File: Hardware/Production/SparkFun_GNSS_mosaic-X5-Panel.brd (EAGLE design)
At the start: 155.2 x 115.8 mm, 754 parts, among them J10 USB Female Type C Connector, J13 MICROSD, J21 USB Female Type C Connector, J23 MICROSD, J3 MICROSD, J31 USB Female Type C Connector, J33 MICROSD, J5 USB Female Type C Connector, Q1 20V/0.2A/8MHz/1.2Ω/1Vth, Q2 20V/0.2A/8MHz/1.2Ω/1Vth, Q3 20V/0.2A/8MHz/1.2Ω/1Vth, Q9 20V/0.2A/8MHz/1.2Ω/1Vth, T1 RFCMF1220100M4T, T2 RFCMF1220100M4T, T3 RFCMF1220100M4T, T4 RFCMF1220100M4T, U1 MOSAIC-X5X5, U10 3.3V, U11 MOSAIC-X5X5, U12 SN74AHC1G125DBVR, U2 SN74AHC1G125DBVR, U3 3.3V, U4 MOSAIC-X5X5, U5 3.3V, U6 SN74AHC1G125DBVR, U7 3.3V, U8 MOSAIC-X5X5, U9 SN74AHC1G125DBVR

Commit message: Add v11 panel.
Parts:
- added D45: RED, SparkFun-LED:LED-0603
- added D46: GREEN, SparkFun-LED:LED-0603
- added D47: ESD Diode, SparkFun-DiscreteSemi:SOT-23-6
- added D48, D49: 3A/10V/280mV, SparkFun-DiscreteSemi:SOD-323
- added D50: BLUE, SparkFun-LED:LED-0603
- added D51: WHITE, SparkFun-LED:LED-0603
- added D52, D53, D54, D55, D56: PESDXL4UGUG, SparkFun-DiscreteSemi:SOT353
- added R69, R70: 2.2k, SparkFun-Resistors:0603
- added R71: 0, SparkFun-Resistors:0603
- added R72: 10k, SparkFun-Resistors:0603
- D12: value PESD0402 -> PESDXL4UGUG; device SparkFun-DiscreteSemi:0402-TIGHT -> SparkFun-DiscreteSemi:SOT353
- D13, D24: value Yellow -> PESDXL4UGUG; device SparkFun-LED:LED-0603 -> SparkFun-DiscreteSemi:SOT353
- D14, D25: value RED -> PESDXL4UGUG; device SparkFun-LED:LED-0603 -> SparkFun-DiscreteSemi:SOT353
- D15: value GREEN -> PESD0402; device SparkFun-LED:LED-0603 -> SparkFun-DiscreteSemi:0402-TIGHT
- D16: value ESD Diode -> Yellow; device SparkFun-DiscreteSemi:SOT-23-6 -> SparkFun-LED:LED-0603
- D17: value 3A/10V/280mV -> RED; device SparkFun-DiscreteSemi:SOD-323 -> SparkFun-LED:LED-0603
- D18: value 3A/10V/280mV -> GREEN; device SparkFun-DiscreteSemi:SOD-323 -> SparkFun-LED:LED-0603
- D19: value BLUE -> ESD Diode; device SparkFun-LED:LED-0603 -> SparkFun-DiscreteSemi:SOT-23-6
- D20: value WHITE -> 3A/10V/280mV; device SparkFun-LED:LED-0603 -> SparkFun-DiscreteSemi:SOD-323
- D21: value PESDXL4UGUG -> 3A/10V/280mV; device SparkFun-DiscreteSemi:SOT353 -> SparkFun-DiscreteSemi:SOD-323
- D22: value PESDXL4UGUG -> BLUE; device SparkFun-DiscreteSemi:SOT353 -> SparkFun-LED:LED-0603
- D23: value PESD0402 -> WHITE; device SparkFun-DiscreteSemi:0402-TIGHT -> SparkFun-LED:LED-0603
- D26: value GREEN -> PESDXL4UGUG; device SparkFun-LED:LED-0603 -> SparkFun-DiscreteSemi:SOT353
- D27, D38: value ESD Diode -> PESDXL4UGUG; device SparkFun-DiscreteSemi:SOT-23-6 -> SparkFun-DiscreteSemi:SOT353
- D28, D39, D40: value 3A/10V/280mV -> PESDXL4UGUG; device SparkFun-DiscreteSemi:SOD-323 -> SparkFun-DiscreteSemi:SOT353
- D29: value 3A/10V/280mV -> PESD0402; device SparkFun-DiscreteSemi:SOD-323 -> SparkFun-DiscreteSemi:0402-TIGHT
- D30: value BLUE -> Yellow
- D31: value WHITE -> RED
- D32: value PESDXL4UGUG -> GREEN; device SparkFun-DiscreteSemi:SOT353 -> SparkFun-LED:LED-0603
- D33: value PESDXL4UGUG -> ESD Diode; device SparkFun-DiscreteSemi:SOT353 -> SparkFun-DiscreteSemi:SOT-23-6
- D34: value PESD0402 -> 3A/10V/280mV; device SparkFun-DiscreteSemi:0402-TIGHT -> SparkFun-DiscreteSemi:SOD-323
- D35: value Yellow -> 3A/10V/280mV; device SparkFun-LED:LED-0603 -> SparkFun-DiscreteSemi:SOD-323
- D36: value RED -> BLUE
- D37: value GREEN -> WHITE
- D41: value BLUE -> PESDXL4UGUG; device SparkFun-LED:LED-0603 -> SparkFun-DiscreteSemi:SOT353
- D42: value WHITE -> PESDXL4UGUG; device SparkFun-LED:LED-0603 -> SparkFun-DiscreteSemi:SOT353
- D43: value PESDXL4UGUG -> PESD0402; device SparkFun-DiscreteSemi:SOT353 -> SparkFun-DiscreteSemi:0402-TIGHT
- D44: value PESDXL4UGUG -> Yellow; device SparkFun-DiscreteSemi:SOT353 -> SparkFun-LED:LED-0603
- R14, R34: value 5.1k -> 10k
- R18, R35: value 2.2k -> 5.1k
- R19: value 1k -> 2.2k
- R20: value 330 -> 1k
- R21, R39, R59: value 10k -> 330
- R24, R41, R60, R65: value 1k -> 10k
- R25, R30, R50: value 2.2k -> 1k
- R26, R57: value 10k -> 2.2k
- R27, R45: value 169K -> 10k
- R29, R48: value 1k -> 169K
- R32, R51: value 0 -> 2.2k
- R33, R53: value 5.1k -> 0
- R36, R55: value 1k -> 5.1k
- R37: value 330 -> 2.2k
- R38, R43, R58: value 10k -> 1k
- R42, R54, R61: value 2.2k -> 10k
- R44, R64: value 169K -> 2.2k
- R49, R66, R67: value 2.2k -> 169K
- R52: value 5.1k -> 2.2k
- R56: value 330 -> 5.1k
- R63: value 169K -> 1k
- R68: value 0 -> 1k
- U$105: device output:#RTS_#5 -> output:COM40
- U$120: device output:#LOG#5 -> output:COM10
- U$126: device output:#LOG_LED_#5 -> output:#3#3V#1
- U$127: device output:#PMIC_#6 -> output:#GND#0
- U$128: device output:#GP_LED_#4 -> output:#3#3V#1
- U$129: device output:#RDY_#3 -> output:#GND#0
- U$139: device output:#RDY#3 -> output:##RST##2
- U$148: device output:#EVENTA_#9 -> output:#GP_LED#4
- U$149: device output:#EVENTB#11 -> output:#PMIC#6
- U$151: device output:#GP1_#2 -> output:#RDY#3
- U$153: device output:#GP2_#3 -> output:#VIN#1
- U$155: device output:#LOG_BTN_#5 -> output:#VUSB#0
- U$157: device output:#PPS_#7 -> output:#V_BAT#7
- U$161, U$269, U$377: device output:#RDY_#3 -> output:#_#RST##2
- U$162, U$270, U$378: device output:#VIN#1 -> output:L1#2#50
- U$163, U$271, U$379: device output:#VUSB#0 -> output:_ACTIVE_ANT1
- U$164, U$272, U$380: device output:#V_BAT#7 -> output:TIME0
- U$165, U$273, U$381: device output:#_#RST##2 -> output:PULSE1
- U$166, U$274, U$382: device output:#LOG_LED_#5 -> output:GNSS1
- U$167, U$275, U$383: device output:#PMIC_#6 -> output:TRIBAND2
- U$168, U$276, U$384: device output:#GP_LED_#4 -> output:#GP_LED#3
- U$169, U$277, U$385: device output:L1#2#50 -> output:#LOG_LED#2
- U$17: device output:#_RTK#0 -> output:#EVENTA#0
- U$170, U$278, U$386: device output:_ACTIVE_ANT1 -> output:#PPS_LED#1
- U$171, U$279, U$387: device output:TIME0 -> output:#PWR_LED#0
- U$172, U$280, U$388: device output:PULSE1 -> output:#V_BAT#4
- U$173, U$281, U$389: device output:GNSS1 -> output:#A#8
- U$174, U$282, U$390: device output:TRIBAND2 -> output:#B#10
- U$175, U$283, U$391: device output:#GP_LED#3 -> output:#GP1#0
- U$176, U$284, U$392: device output:#LOG_LED#2 -> output:#GP2#1
- U$177, U$285, U$393: device output:#PPS_LED#1 -> output:#LOG#4
- U$178, U$286, U$394: device output:#PWR_LED#0 -> output:#PPS#6
- U$179, U$287, U$395: device output:#V_BAT#4 -> output:GNSS_1
- U$180, U$288, U$396: device output:#A#8 -> output:TRIBAND_2
- U$181, U$289, U$397: device output:#B#10 -> output:MEAS0
- U$182, U$290, U$398: device output:#EVENTA_#9 -> output:C4
- U$183, U$291, U$399: device output:#EVENTB#11 -> output:D#2
- U$184, U$292, U$400: device output:#GP1#0 -> output:D#3
- U$185, U$293, U$401: device output:#GP1_#2 -> output:G0
- U$186, U$294, U$402: device output:#GP2#1 -> output:R5
- U$187, U$295, U$403: device output:#GP2_#3 -> output:RX7
- U$188, U$296, U$404: device output:#LOG#4 -> output:TX6
- U$189, U$297, U$405: device output:#LOG_BTN_#5 -> output:V8
- U$190, U$298, U$406: device output:#PPS#6 -> output:COM30
- U$191, U$299, U$407: device output:#PPS_#7 -> output:MOSAIC#X50
- U$192, U$300, U$408: device output:GNSS_1 -> output:MOSAIC#X5_0
- U$193, U$301, U$409: device output:TRIBAND_2 -> output:V0
- U$194, U$302, U$410: device output:MEAS0 -> output:G1
- U$195, U$303, U$411: device output:C4 -> output:#RTK#0
- U$196, U$304, U$412: device output:D#2 -> output:3V30
- U$197, U$305, U$413: device output:D#3 -> output:5V0
- U$198, U$306, U$414: device output:G0 -> output:#ANT_V#0
- U$199, U$307, U$415: device output:R5 -> output:#RTK_LED#0
- U$200, U$308, U$416: device output:RX7 -> output:RTK0
- U$201, U$309, U$417: device output:TX6 -> output:PVT0
- U$202, U$310, U$418: device output:V8 -> output:#GP1_#0
- U$203, U$311, U$419: device output:COM30 -> output:#GP2_#0
- U$204, U$312, U$420: device output:MOSAIC#X50 -> output:#PPS_#0
- U$205, U$313, U$421: device output:MOSAIC#X5_0 -> output:#LOG_BTN#0
- U$206, U$314, U$422: device output:V0 -> output:#LOG_L#0
- U$207, U$315, U$423: device output:G1 -> output:#RDY#0
- U$208, U$316, U$424: device output:#RTK#0 -> output:#GP_LED#0
- U$209, U$317, U$425: device output:#_RTK#0 -> output:#LOG_LED#0
- U$210, U$318, U$426: device output:3V30 -> output:#PMIC#0
- U$211, U$319, U$427: device output:5V0 -> output:#RTS#0
- U$212, U$320, U$428: device output:#ANT_V#0 -> output:#RTS#0
- U$213, U$321, U$429: device output:#RTK_LED#0 -> output:#RTK_#0
- U$214, U$322, U$430: device output:RTK0 -> output:#EVENTA#0
- U$215, U$323, U$431: device output:PVT0 -> output:#EVENTB#0
- U$216, U$324, U$432: device output:MADE_IN_AMERICA0 -> output:MADE_IN_THE_USA0
- U$239, U$347: device output:#RTS_#5 -> output:#RX_#2
- U$240, U$348: device output:#RX_#2 -> output:#TX_#3
- U$241, U$349: device output:#TX_#3 -> output:#CTS#4
- U$242, U$350: device output:#CTS#4 -> output:#RTS#5
- U$243, U$351: device output:#RTS#5 -> output:#RX#2
- U$244, U$352: device output:#RX#2 -> output:#TX#3
- U$245, U$353: device output:#TX#3 -> output:#CTS_#4
- U$246, U$354: device output:#CTS_#4 -> output:#RX_#2
- U$247, U$355: device output:#RTS_#5 -> output:#TX_#3
- U$248, U$356: device output:#RX_#2 -> output:#RX#2
- U$249, U$357: device output:#TX_#3 -> output:#TX#3
- U$250, U$358: device output:#RX#2 -> output:#RX_#2
- U$251, U$359: device output:#TX#3 -> output:#TX_#3
- U$252, U$360, U$54: device output:#RX_#2 -> output:COM20
- U$253, U$361: device output:#TX_#3 -> output:COM40
- U$254, U$362: device output:COM20 -> output:COM10
- U$255, U$363: device output:COM40 -> output:#3#3V#1
- U$256, U$364: device output:COM10 -> output:#GND#0
- U$259, U$367: device output:#3#3V#1 -> output:##RST##2
- U$260, U$368: device output:#GND#0 -> output:#GP_LED#4
- U$261, U$369: device output:##RST##2 -> output:#PMIC#6
- U$262, U$370: device output:#GP_LED#4 -> output:#RDY#3
- U$263, U$371: device output:#LOG#5 -> output:#VIN#1
- U$264, U$372: device output:#PMIC#6 -> output:#VUSB#0
- U$265, U$373: device output:#RDY#3 -> output:#V_BAT#7
- U$30: device output:MADE_IN_AMERICA0 -> output:#GP1_#0
- U$33: device output:L1#2#50 -> output:#GP2_#0
- U$34: device output:_ACTIVE_ANT1 -> output:#PPS_#0
- U$35: device output:RST0 -> output:#LOG_BTN#0
- U$36: device output:LOG0 -> output:#LOG_L#0
- U$37: device output:LOG2 -> output:#RDY#0
- U$38: device output:PPS0 -> output:#GP_LED#0
- U$39: device output:PWR3 -> output:#LOG_LED#0
- U$40: device output:COM30 -> output:#PMIC#0
- U$41: device output:COM20 -> output:#RTS#0
- U$42: device output:COM10 -> output:#RTS#0
- U$43: device output:COM40 -> output:#RTK_#0
- U$44: device output:#3#3V#1 -> output:#EVENTB#0
- U$45: device output:#CTS#4 -> output:MADE_IN_THE_USA0
- U$46: device output:#GND#0 -> output:L1#2#50
- U$47: device output:#RTS#5 -> output:_ACTIVE_ANT1
- U$48: device output:#RX#2 -> output:RST0
- U$49: device output:#TX#3 -> output:LOG0
- U$50: device output:#3#3V#1 -> output:LOG2
- U$51: device output:#CTS_#4 -> output:PPS0
- U$52: device output:#GND#0 -> output:PWR3
- U$53: device output:#RTS_#5 -> output:COM30
- U$55: device output:#TX_#3 -> output:COM10
- U$56: device output:#CTS#4 -> output:COM40
- U$57: device output:#RTS#5 -> output:#3#3V#1
- U$58: device output:#RX#2 -> output:#CTS#4
- U$59, U$65: device output:#TX#3 -> output:#GND#0
- U$60: device output:#CTS_#4 -> output:#RTS#5
- U$61: device output:#RTS_#5 -> output:#RX#2
- U$62: device output:#RX_#2 -> output:#TX#3
- U$63: device output:#TX_#3 -> output:#3#3V#1
- U$64: device output:#RX#2 -> output:#CTS_#4
- U$68: device output:COM20 -> output:#CTS#4
- U$70: device output:COM40 -> output:#RTS#5
- U$71: device output:COM10 -> output:#RX#2
- U$72: device output:#3#3V#1 -> output:#TX#3
- U$73: device output:#GND#0 -> output:#CTS_#4
- U$74: device output:#3#3V#1 -> output:#RX_#2
- U$75: device output:#GND#0 -> output:#TX_#3
- U$76: device output:##RST##2 -> output:#RX#2
- U$77: device output:#GP_LED#4 -> output:#TX#3
- U$78: device output:#LOG#5 -> output:#RX_#2
- U$86: device output:#PMIC#6 -> output:#TX_#3
- U$96: device output:#RTS_#5 -> output:COM20
- moved D28 121.9 mm to (108.5, 7.62), turned to 270 degrees
- moved R34 120.6 mm to (116.1, 7.62), turned to 0 degrees
- moved D35 112.9 mm to (8.89, 67.8), turned to 180 degrees
- moved D34 112.6 mm to (8.89, 78.0), turned to 180 degrees
- moved D13 103.8 mm to (21.6, 7.62), turned to 270 degrees
- moved D41 102.5 mm to (21.6, 58.9), turned to 270 degrees
- moved D26 101.5 mm to (98.3, 7.62), turned to 270 degrees
- moved R33 100.6 mm to (109.7, 43.2), turned to 270 degrees
- moved D27 94.8 mm to (88.1, 7.62), turned to 270 degrees
- moved D12 93.5 mm to (31.8, 7.62)
- moved U$33 90.7 mm to (43.2, 3.68), flipped to the bottom, turned to 270 degrees
- moved U$37 88.1 mm to (33.0, 46.7), flipped to the bottom, turned to 270 degrees
- moved D14 86.3 mm to (41.9, 7.62), turned to 270 degrees
- moved U$38 85.5 mm to (35.6, 45.2), flipped to the bottom, turned to 270 degrees
- moved U$39 83.3 mm to (38.1, 44.7), flipped to the bottom, turned to 270 degrees
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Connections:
- removed net ICM-20948-LV_#_1.8V: Q9.1, R46.2
- removed net ICM-20948-LV_#_1.8V1: Q1.1, R30.2
- removed net ICM-20948-LV_#_1.8V2: Q2.1, R49.2
- removed net ICM-20948-LV_#_1.8V3: Q3.1, R66.2
- net !RESET!: now also D9.3
- net !RESET!1: now also D24.3
- net !RESET!2: now also D38.3
- net !RESET!3: now also D52.3
- net 1.8V: now also Q9.1, R46.2
- net 1.8V1: now also Q1.1, R22.2, R31.2; no longer R21.2
- net 1.8V2: now also Q2.1, R40.2, R51.2; no longer R38.2
- net 1.8V3: now also Q3.1, R60.2, R69.2; no longer R57.2
- net 3.3V: now also R14.2
- net 3.3V1: now also R24.2, R27.2, R32.2, R34.2; no longer R22.2, R26.2, R31.2
- net 3.3V2: now also R41.2, R42.2, R45.2, R52.2, R54.2; no longer R39.2, R40.2, R43.2, R50.2
- net 3.3V3: now also R61.2, R65.2, R70.2, R72.2; no longer R58.2, R59.2, R67.2
- net ANT_V1: now also R33.1; no longer R32.1
- net ANT_V2: now also R53.1; no longer R51.1
- net ANT_V3: now also R71.1; no longer R68.1
- net CC3: now also R18.2; no longer R15.2
- net CC4: now also R15.2; no longer R14.2
- net CC5: now also R36.2; no longer R34.2
- net CC6: now also R35.2; no longer R33.2
- net CC7: now also R56.2; no longer R53.2
- net CC8: now also R55.2; no longer R52.2
- net COM1_CTS: now also D13.4
- net COM1_CTS1: now also D27.4
- net COM1_CTS2: now also D41.4
- net COM1_CTS3: now also D55.4
- net COM1_RTS: now also D13.3
- net COM1_RTS1: now also D27.3
- net COM1_RTS2: now also D41.3
- net COM1_RTS3: now also D55.3
- net COM1_RX: now also D13.1
- net COM1_RX1: now also D27.1
- net COM1_RX2: now also D41.1
- net COM1_RX3: now also D55.1
- net COM1_TX: now also D13.5
- net COM1_TX1: now also D27.5
- net COM1_TX2: now also D41.5
- net COM1_TX3: now also D55.5
- net COM2_CTS: now also D12.5
- net COM2_CTS1: now also D26.5
- net COM2_CTS2: now also D40.5
- net COM2_CTS3: now also D54.5
- net COM2_RTS: now also D12.1
- net COM2_RTS1: now also D26.1
- net COM2_RTS2: now also D40.1
- net COM2_RTS3: now also D54.1
- net COM2_RX: now also D12.3
- net COM2_RX1: now also D26.3
- net COM2_RX2: now also D40.3
- net COM2_RX3: now also D54.3
- net COM2_TX: now also D12.4
- net COM2_TX1: now also D26.4
- net COM2_TX2: now also D40.4
- net COM2_TX3: now also D54.4
- net COM3_CTS1: now also D25.5; no longer D22.5
- net COM3_CTS2: now also D39.5; no longer D33.5
- net COM3_CTS3: now also D53.5; no longer D44.5
- net COM3_RTS1: now also D25.4; no longer D22.4
- net COM3_RTS2: now also D39.4; no longer D33.4
- net COM3_RTS3: now also D53.4; no longer D44.4
- net COM3_RX1: now also D25.1; no longer D22.1
- net COM3_RX2: now also D39.1; no longer D33.1
- net COM3_RX3: now also D53.1; no longer D44.1
- net COM3_TX1: now also D25.3; no longer D22.3
- net COM3_TX2: now also D39.3; no longer D33.3
- net COM3_TX3: now also D53.3; no longer D44.3
- net COM4_RX: now also D14.1
- net COM4_RX1: now also D28.1
- net COM4_RX2: now also D42.1
- net COM4_RX3: now also D56.1
- net COM4_TX: now also D14.3
- net COM4_TX1: now also D28.3
- net COM4_TX2: now also D42.3
- net COM4_TX3: now also D56.3
- net EVENTA1: now also R28.2; no longer R27.2
- net EVENTA2: now also R48.2; no longer R44.2
- net EVENTA3: now also R66.2; no longer R63.2
- net EVENTB1: now also R29.2; no longer R28.2
- net EVENTB2: now also R49.2; no longer R45.2
- net EVENTB3: now also R67.2; no longer R64.2
- net GND: now also D12.2, D13.2, D14.2
- net GND1: now also D15.2, D16.C, D17.C, D18.C, D19.2, D22.C, D23.C, D24.2, D25.2, D26.2, D27.2, D28.2, R18.1; no longer D12.2, D13.C, D14.C, D15.C, D16.2, D19.C, D20.C, D21.2, D22.2, R14.1
- net GND2: now also D29.2, D32.C, D36.C, D37.C, D38.2, D39.2, D40.2, D41.2, D42.2, R35.1, R36.1; no longer D23.2, D24.C, D25.C, D26.C, D27.2, D32.2, R33.1, R34.1
- net GND3: now also D44.C, D45.C, D46.C, D47.2, D50.C, D51.C, D52.2, D53.2, D54.2, D55.2, D56.2, R55.1, R56.1; no longer D34.2, D35.C, D36.C, D37.C, D38.2, D41.C, D42.C, D44.2, R52.1, R53.1
- net GP1: now also D14.4
- net GP2: now also D14.5
- net GP3: now also D28.4
- net GP4: now also D28.5
- net GP5: now also D42.4
- net GP6: now also D42.5
- net GP7: now also D56.4
- net GP8: now also D56.5
- net GPS_ANT2: now also D15.1; no longer D12.1
- net GPS_ANT3: now also D29.1; no longer D23.1
- net GPS_ANT4: now also D43.1; no longer D34.1
- net LOG_BTN: now also R14.1
- net LOG_BTN1: now also R25.2, R34.1; no longer R24.2
- net LOG_BTN2: now also R43.2, R54.1; no longer R41.2
- net LOG_BTN3: now also R63.2, R72.1; no longer R60.2
- net MEAS1: now also D20.C, D21.C; no longer D17.C, D18.C
- net MEAS2: now also D34.C, D35.C; no longer D28.C, D29.C
- net MEAS3: now also D48.C, D49.C; no longer D39.C, D40.C
- net N$13: now also D16.A, R19.1; no longer D13.A, R18.1
- net N$18: now also R19.2; no longer R18.2
- net N$19: now also D17.A, R20.1; no longer D14.A, R19.1
- net N$21: now also D18.A, R21.1; no longer D15.A, R20.1
- net N$22: now also R21.2; no longer R20.2
- net N$23: now also R20.2; no longer R19.2
- net N$27: now also R22.1; no longer R21.1
- net N$28: now also R25.1; no longer R24.1
- net N$29: now also D22.A, R26.1; no longer D19.A, R25.1
- net N$30: now also R26.2; no longer R25.2
- net N$32: now also R27.1; no longer R26.1
- net N$33: now also R28.1; no longer R27.1
- net N$34: now also R29.1; no longer R28.1
- net N$35: now also D23.A, R30.1; no longer D20.A, R29.1
- net N$36: now also R30.2; no longer R29.2
- net N$37: now also D30.A, R37.1; no longer D24.A, R35.1
- net N$38: now also R37.2; no longer R35.2
- net N$39: now also D31.A, R38.1; no longer D25.A, R36.1
- net N$40: now also D32.A, R39.1; no longer D26.A, R37.1
- net N$41: now also R39.2; no longer R37.2
- net N$42: now also R38.2; no longer R36.2
- net N$45: now also R40.1; no longer R38.1
- net N$46: now also R43.1; no longer R41.1
- net N$47: now also D36.A, R44.1; no longer D30.A, R42.1
- net N$48: now also R44.2; no longer R42.2
- net N$50: now also R45.1; no longer R43.1
- net N$51: now also R48.1; no longer R44.1
- net N$52: now also R49.1; no longer R45.1
- net N$53: now also D37.A, R50.1; no longer D31.A, R48.1
- net N$54: now also R50.2; no longer R48.2
- net N$55: now also D44.A, R57.1; no longer D35.A, R54.1
- net N$56: now also R57.2; no longer R54.2
- net N$57: now also D45.A, R58.1; no longer D36.A, R55.1
- net N$58: now also D46.A, R59.1; no longer D37.A, R56.1
- net N$59: now also R59.2; no longer R56.2
- net N$60: now also R58.2; no longer R55.2
- net N$63: now also R60.1; no longer R57.1
- net N$64: now also R63.1; no longer R60.1
- net N$65: now also D50.A, R64.1; no longer D41.A, R61.1
- net N$66: now also R64.2; no longer R61.2
- net N$68: now also R65.1; no longer R62.1
- net N$69: now also R66.1; no longer R63.1
- net N$70: now also R67.1; no longer R64.1
- net N$71: now also D51.A, R68.1; no longer D42.A, R65.1
- net N$72: now also R68.2; no longer R65.2
- net PPS_1: now also R32.1; no longer R31.1
- net PPS_1V1: now also R31.1; no longer R30.1
- net PPS_1V2: now also R51.1; no longer R49.1
- net PPS_1V3: now also R69.1; no longer R66.1
- net PPS_2: now also R52.1; no longer R50.1
- net PPS_4: now also R70.1; no longer R67.1
- net SD_CLK1: now also D24.5; no longer D21.5
- net SD_CLK2: now also D38.5; no longer D32.5
- net SD_CLK3: now also D52.5; no longer D43.5
- net SD_CMD1: now also D24.4, R23.1; no longer D21.4, R22.1
- net SD_CMD2: now also D38.4, R41.1; no longer D32.4, R39.1
- net SD_CMD3: now also D52.4, R61.1; no longer D43.4, R58.1
- net SD_DATA1: now also D24.1, R24.1; no longer D21.1, R23.1
- net SD_DATA2: now also D38.1, R42.1; no longer D32.1, R40.1
- net SD_DATA3: now also D52.1, R62.1; no longer D43.1, R59.1
- net USB_D+1: now also D19.6; no longer D16.6
- net USB_D+2: now also D33.6; no longer D27.6
- net USB_D+3: now also D47.6; no longer D38.6
- net USB_D-1: now also D19.4; no longer D16.4
- net USB_D-2: now also D33.4; no longer D27.4
- net USB_D-3: now also D47.4; no longer D38.4
- net VANT1: now also R33.2; no longer R32.2
- net VANT2: now also R53.2; no longer R51.2
- net VANT3: now also R71.2; no longer R68.2
- net VIN1: now also D20.A; no longer D17.A
- net VIN2: now also D34.A; no longer D28.A
- net VIN3: now also D48.A; no longer D39.A
- net V_USB1: now also D19.5, D21.A; no longer D16.5, D18.A
- net V_USB2: now also D33.5, D35.A; no longer D27.5, D29.A
- net V_USB3: now also D47.5, D49.A; no longer D38.5, D40.A
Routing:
- net 1.8V1: track 6.61 -> 32.7 mm, vias 0 -> 2
- net 1.8V3: track 6.61 -> 32.7 mm, vias 0 -> 2
- net 1.8V: track 6.61 -> 32.7 mm, vias 0 -> 2
- net 1.8V2: track 6.61 -> 32.7 mm, vias 0 -> 2
- net 3.3V3: track 169.1 -> 188.7 mm, vias 6 -> 7
- net 3.3V2: track 169.1 -> 188.7 mm, vias 6 -> 7
- net 3.3V1: track 169.1 -> 188.7 mm, vias 6 -> 7
- net 3.3V: track 169.1 -> 188.7 mm, vias 6 -> 7
- net COM2_RX1: track 11.7 -> 23.9 mm, vias 0 -> 1
- net COM2_RX: track 11.7 -> 23.9 mm, vias 0 -> 1
- net COM2_RX3: track 11.7 -> 23.9 mm, vias 0 -> 1
- net COM2_RX2: track 11.7 -> 23.9 mm, vias 0 -> 1
- net COM4_RX1: track 35.4 -> 45.8 mm
- net COM4_RX: track 35.4 -> 45.8 mm
- net COM4_RX3: track 35.4 -> 45.8 mm
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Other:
- board text added: "v11"
- board text removed: "v10"

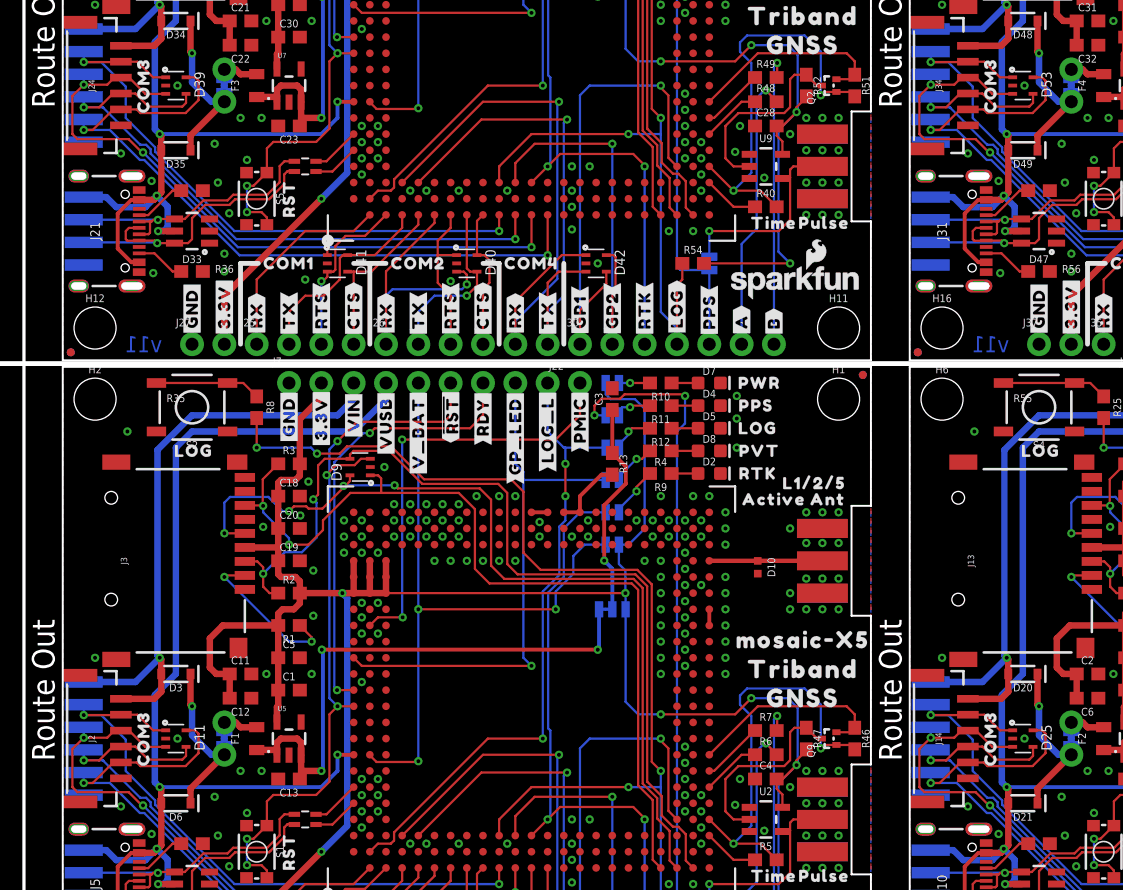
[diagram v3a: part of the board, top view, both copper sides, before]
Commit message: Swap CTS/RTS on COM3 JST connector.
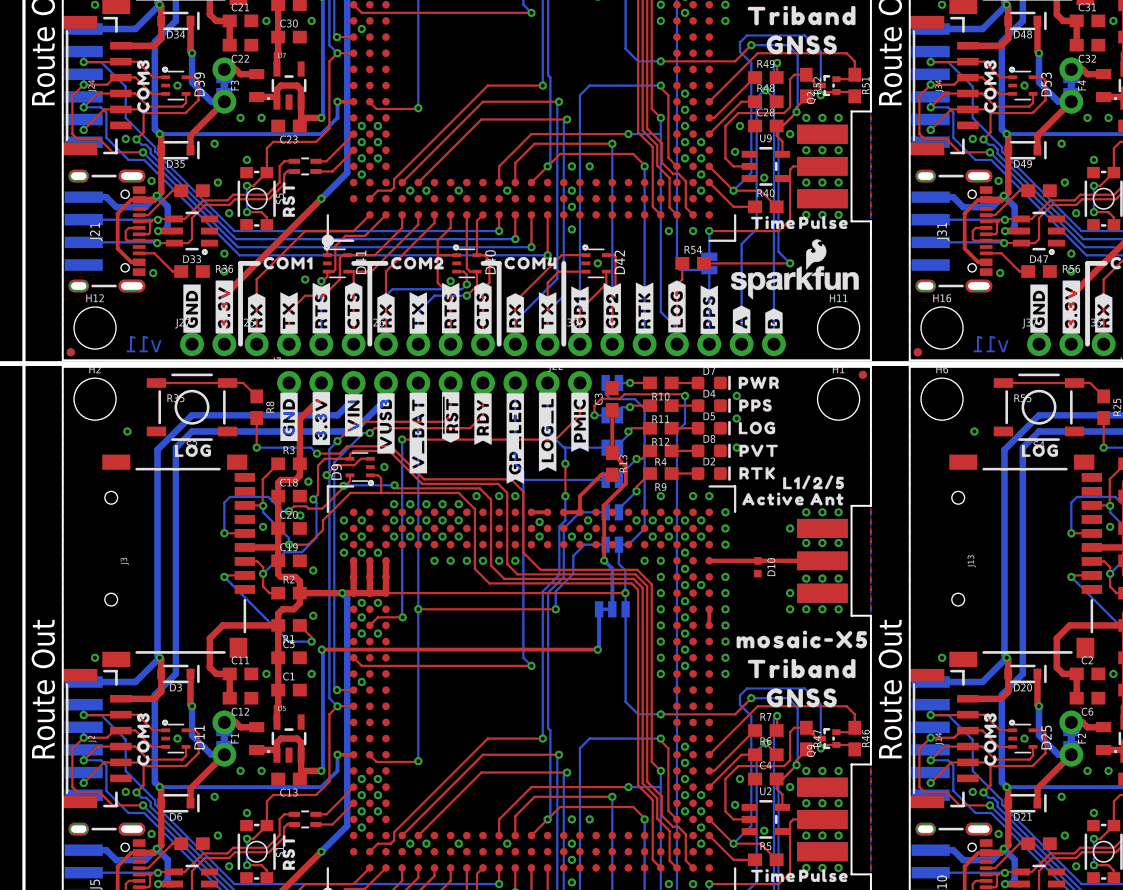
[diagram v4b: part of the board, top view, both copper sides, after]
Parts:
- moved U$402 1.78 mm to (70.7, 70.2)
- moved U$294 1.78 mm to (4.19, 70.2)
- moved U$186 1.78 mm to (70.7, 18.9)
- moved U$12 1.78 mm to (4.19, 18.9)
- moved U$290 1.78 mm to (4.19, 72.0)
- moved U$398 1.78 mm to (70.7, 72.0)
- moved U$182 1.78 mm to (70.7, 20.7)
- moved U$8 1.78 mm to (4.19, 20.7)
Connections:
- net COM3_CTS: now also D11.4, J12.4, J2.4; no longer D11.5, J12.5, J2.5
- net COM3_CTS1: now also D25.4, J14.4, J19.4; no longer D25.5, J14.5, J19.5
- net COM3_CTS2: now also D39.4, J24.4, J29.4; no longer D39.5, J24.5, J29.5
- net COM3_CTS3: now also D53.4, J34.4, J39.4; no longer D53.5, J34.5, J39.5
- net COM3_RTS: now also D11.5, J12.5, J2.5; no longer D11.4, J12.4, J2.4
- net COM3_RTS1: now also D25.5, J14.5, J19.5; no longer D25.4, J14.4, J19.4
- net COM3_RTS2: now also D39.5, J24.5, J29.5; no longer D39.4, J24.4, J29.4
- net COM3_RTS3: now also D53.5, J34.5, J39.5; no longer D53.4, J34.4, J39.4
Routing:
- net COM3_CTS: track 57.4 -> 56.2 mm
- net COM3_CTS1: track 57.4 -> 56.2 mm
- net COM3_CTS3: track 57.4 -> 56.2 mm
- net COM3_CTS2: track 57.4 -> 56.2 mm
- net COM3_RTS: track 50.9 -> 51.1 mm, vias 2 -> 3
- net COM3_RTS2: track 50.9 -> 51.1 mm, vias 2 -> 3
- net COM3_RTS3: track 50.9 -> 51.1 mm, vias 2 -> 3
- net COM3_RTS1: track 50.9 -> 51.1 mm, vias 2 -> 3

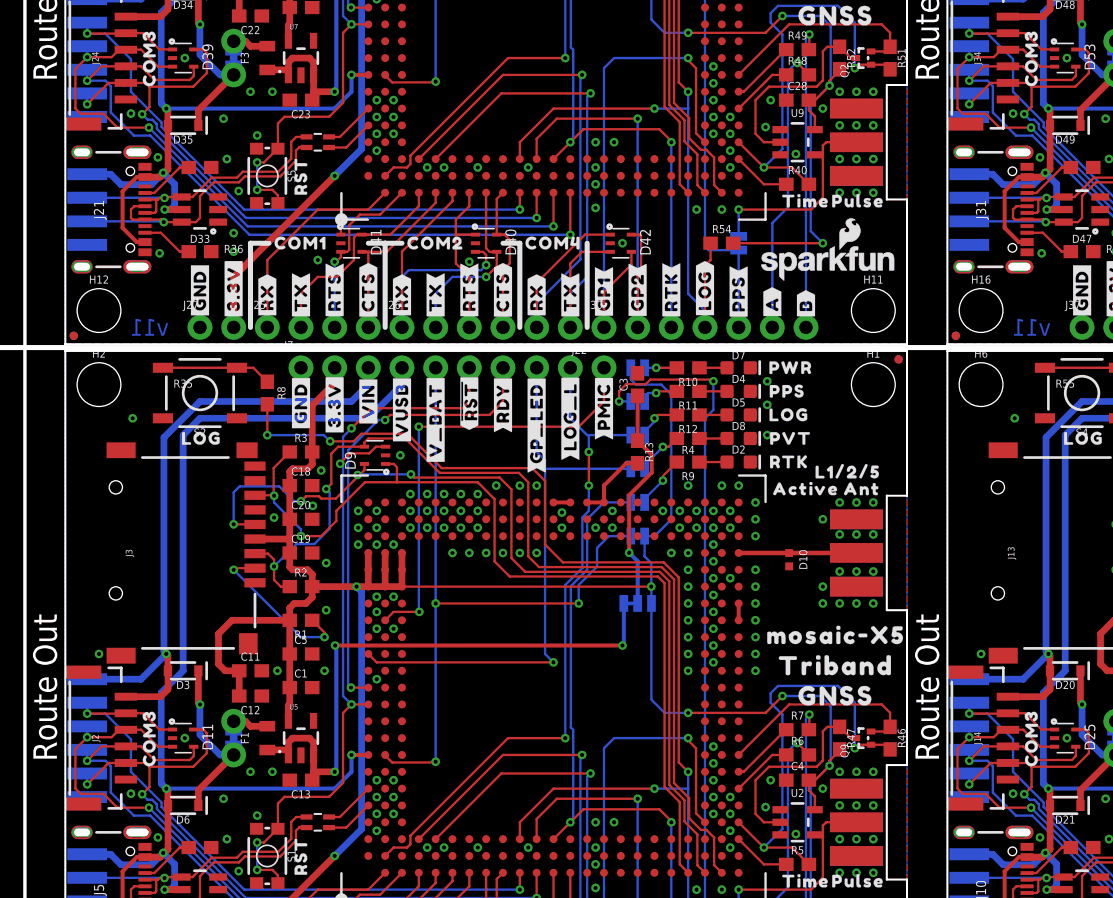
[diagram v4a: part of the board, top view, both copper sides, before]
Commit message: Update board measurements.
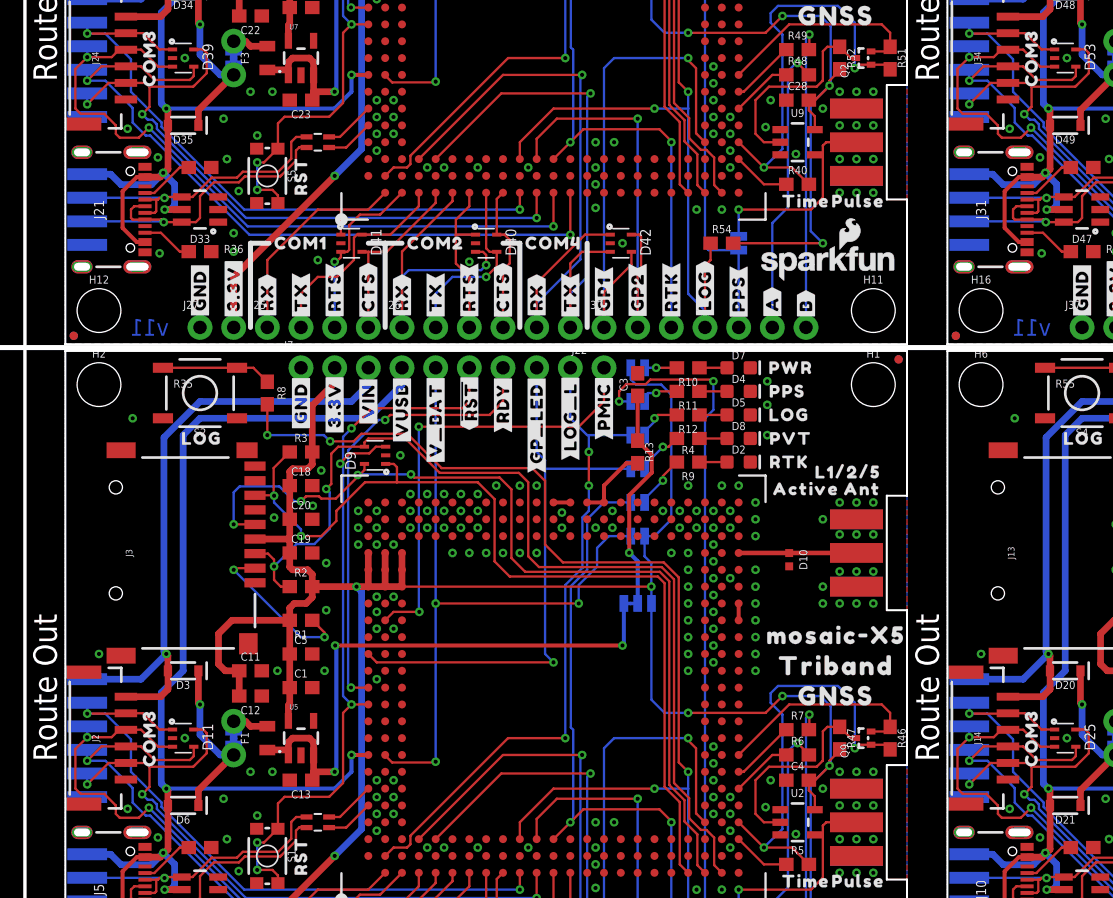
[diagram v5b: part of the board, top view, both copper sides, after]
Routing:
- net COM3_TX: track 54.6 -> 55.6 mm
- net COM3_TX1: track 54.6 -> 55.6 mm
- net COM3_TX2: track 54.6 -> 55.6 mm
- net COM3_TX3: track 54.6 -> 55.6 mm
- net COM3_CTS1: track 56.2 -> 55.6 mm
- net COM3_CTS3: track 56.2 -> 55.6 mm
- net COM3_CTS2: track 56.2 -> 55.6 mm
- net COM3_CTS: track 56.2 -> 55.6 mm

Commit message: Remove "Made in the USA" silk - for foreign PCB manufacture
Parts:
- removed U$216, U$324, U$432, U$45: (no value), output:MADE_IN_THE_USA0
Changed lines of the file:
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@@
 <attribute name="VALUE" x="39.37" y="8.89" size="0.8128" layer="27" rot="R270"/>
 </element>
-<element name="U$45" library="output" package="MADE_IN_THE_USA0" value="" x="19.05" y="11.43" smashed="yes" rot="MR0"/>
 <element name="JP2" library="SparkFun-Aesthetics" package="FIDUCIAL-MICRO" value="FIDUCIALUFIDUCIAL" x="129.413" y="50.165" smashed="yes"/>
 <element name="JP3" library="SparkFun-Aesthetics" package="FIDUCIAL-MICRO" value="FIDUCIALUFIDUCIAL" x="67.183" y="0.635" smashed="yes"/>
@@
 <attribute name="VALUE" x="105.918" y="8.89" size="0.8128" layer="27" rot="R270"/>
 </element>
-<element name="U$216" library="output" package="MADE_IN_THE_USA0" value="" x="85.598" y="11.43" smashed="yes" rot="MR0"/>
 <element name="JP7" library="SparkFun-Aesthetics" package="FIDUCIAL-MICRO" value="FIDUCIALUFIDUCIAL" x="62.865" y="101.473" smashed="yes"/>
 <element name="JP8" library="SparkFun-Aesthetics" package="FIDUCIAL-MICRO" value="FIDUCIALUFIDUCIAL" x="0.635" y="51.943" smashed="yes"/>
@@
 <attribute name="VALUE" x="39.37" y="60.198" size="0.8128" layer="27" rot="R270"/>
 </element>
-<element name="U$324" library="output" package="MADE_IN_THE_USA0" value="" x="19.05" y="62.738" smashed="yes" rot="MR0"/>
 <element name="JP12" library="SparkFun-Aesthetics" package="FIDUCIAL-MICRO" value="FIDUCIALUFIDUCIAL" x="129.413" y="101.473" smashed="yes"/>
 <element name="JP13" library="SparkFun-Aesthetics" package="FIDUCIAL-MICRO" value="FIDUCIALUFIDUCIAL" x="67.183" y="51.943" smashed="yes"/>
@@
 <attribute name="VALUE" x="105.918" y="60.198" size="0.8128" layer="27" rot="R270"/>
 </element>
-<element name="U$432" library="output" package="MADE_IN_THE_USA0" value="" x="85.598" y="62.738" smashed="yes" rot="MR0"/>
 <element name="E$1" library="SparkFun-Aesthetics" package="FIDUCIAL-1X2" value="" x="-5.16381875" y="99.441" smashed="yes"/>
 <element name="E$2" library="SparkFun-Aesthetics" package="FIDUCIAL-1X2" value="" x="-5.16381875" y="99.441" smashed="yes" rot="MR0"/>
